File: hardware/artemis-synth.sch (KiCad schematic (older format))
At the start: 41 parts, among them IC1 ATMEGA328P, J1 AVR-ISP-6, J2 CONN JACK STEREO R/A 3PIN 3.5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, SW1 SWITCH_PUSH_CW, SW10 SWITCH_PUSH_CW, SW2 SWITCH_PUSH_CW, SW3 SWITCH_PUSH_CW, SW4 SWITCH_PUSH_CW, SW5 SWITCH_PUSH_CW, SW6 SWITCH_PUSH_CW, SW7 SWITCH_PUSH_CW, SW8 SWITCH_PUSH_CW, SW9 SWITCH_PUSH_CW, U1 MCP4921

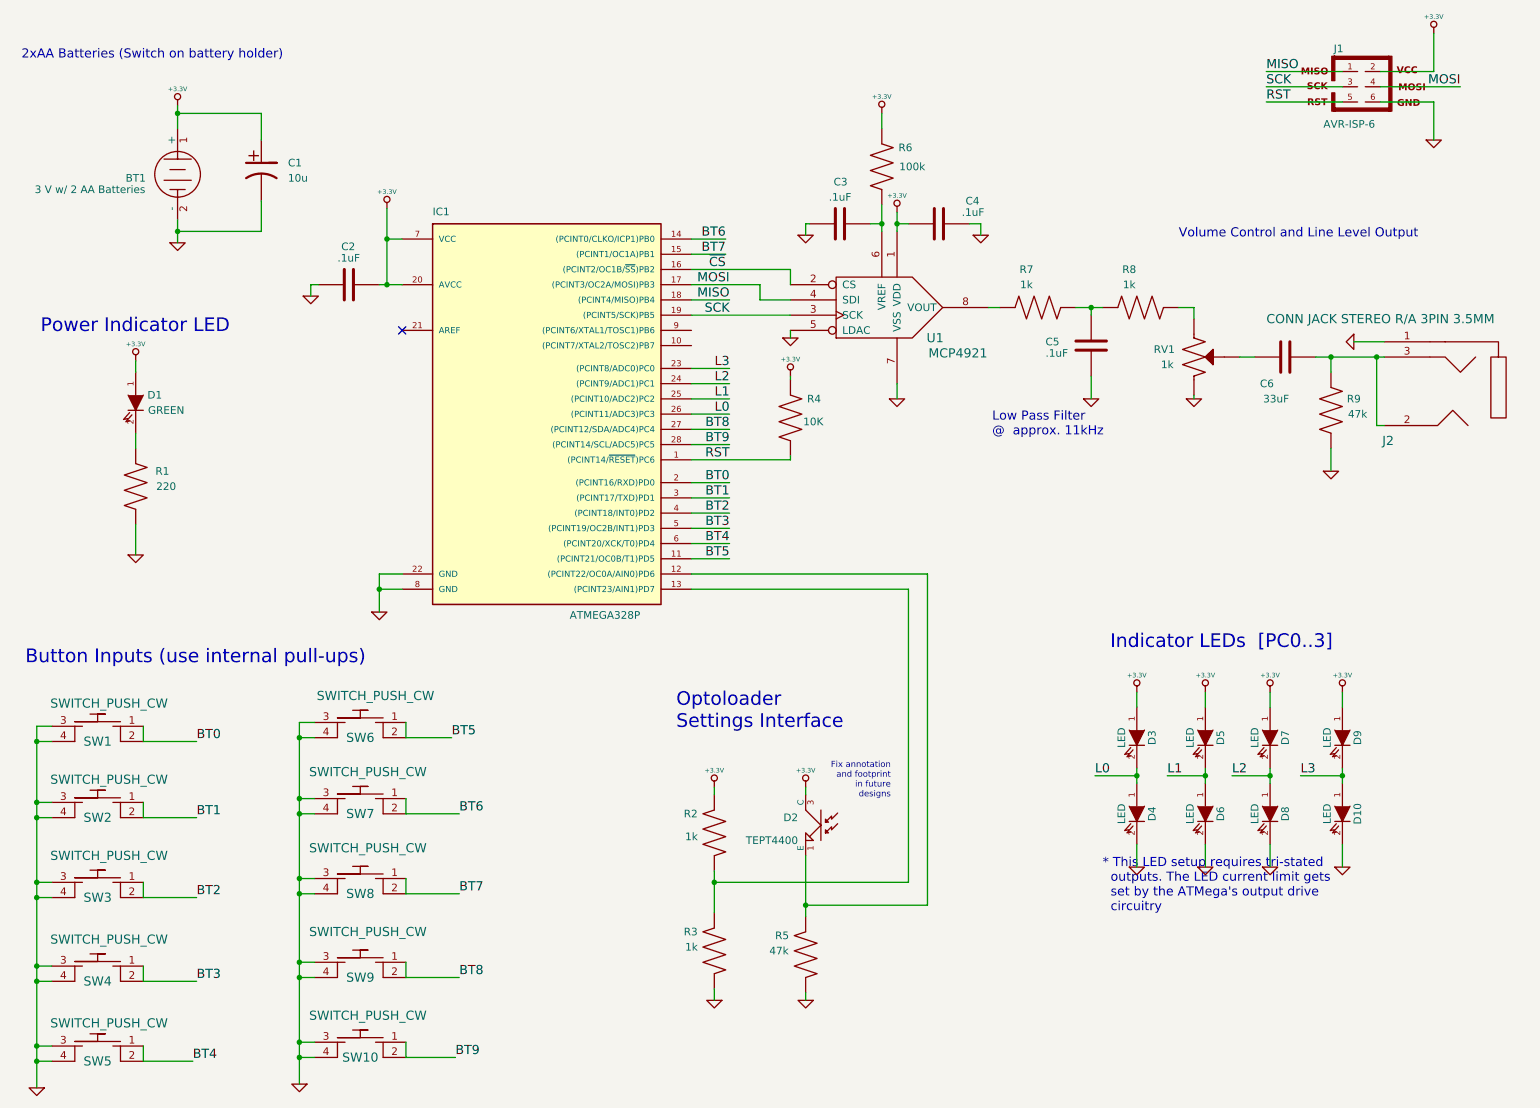
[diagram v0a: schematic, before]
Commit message: Fixed error on D2, in which the collector of the phototransistor was not connected to GND. Also, note that long lead is the Emitter. Fix symbol to make sure it actually represents transistor package correctly...
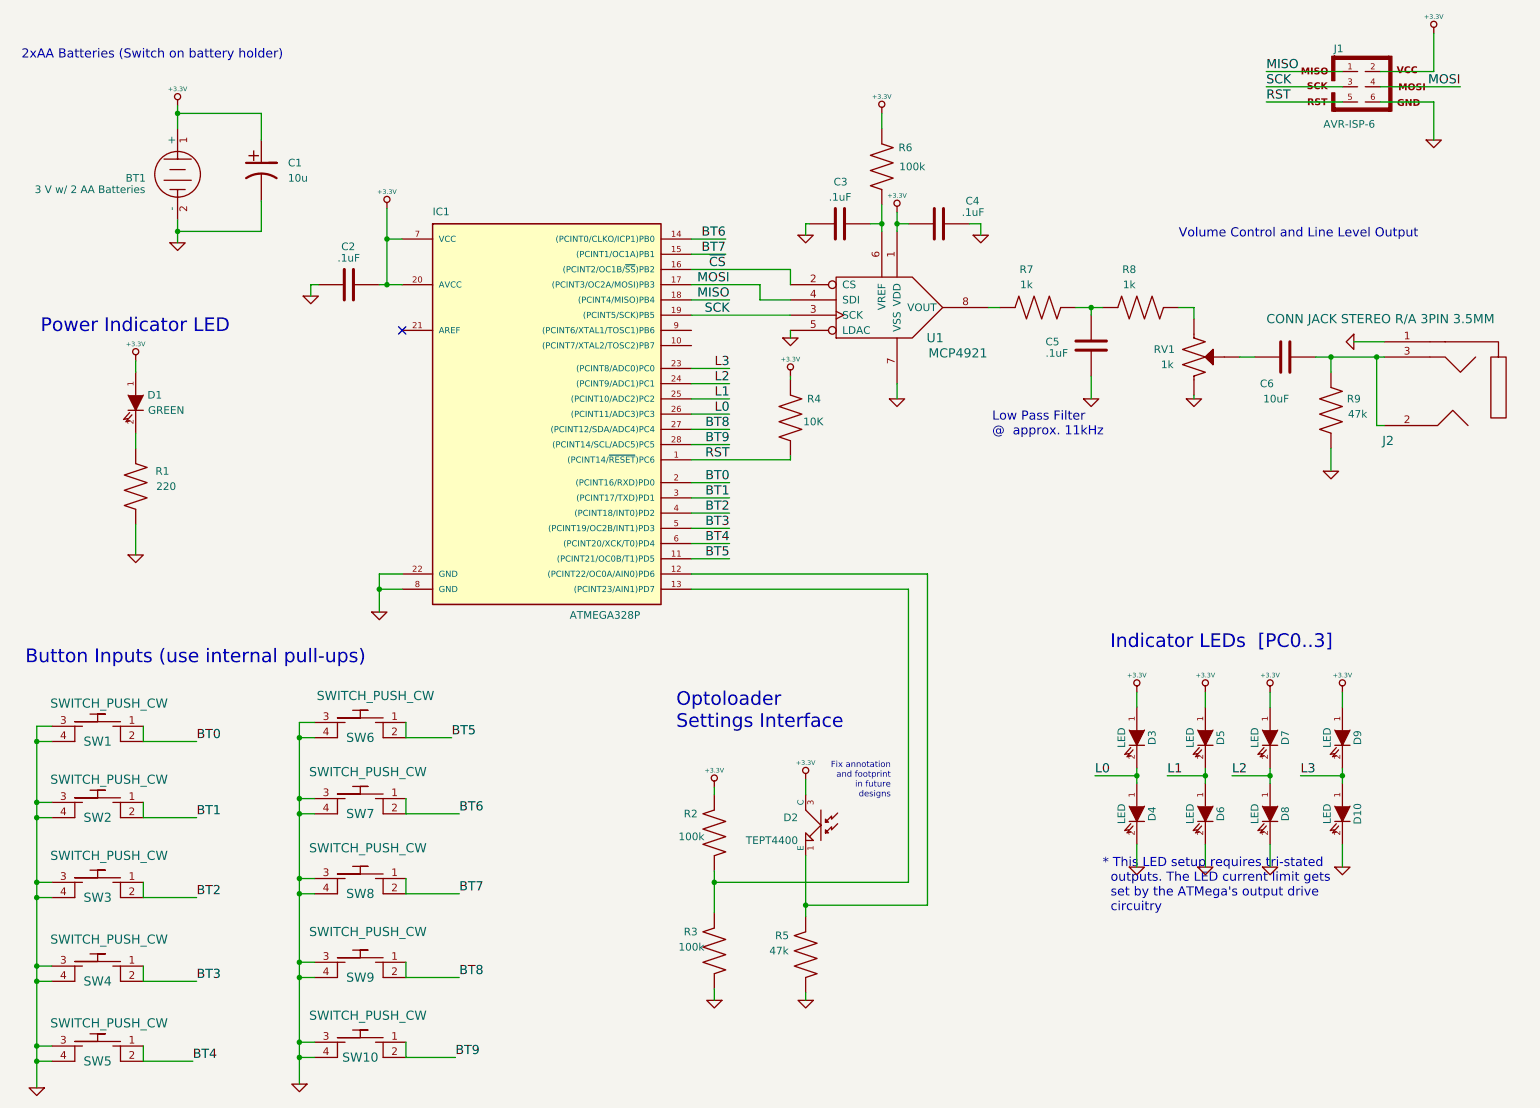
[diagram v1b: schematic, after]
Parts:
- C6: value 33uF -> 10uF
- R2, R3: value 1k -> 100k
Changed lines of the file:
@@
-EESchema Schematic File Version 2  date Fri 05 Jul 2013 12:34:07 PM EDT
+EESchema Schematic File Version 2  date Tue 09 Jul 2013 11:47:29 AM EDT
 LIBS:power
 LIBS:device
@@
 Sheet 1 1
 Title "Artemis Synthesizer"
-Date "5 jul 2013"
+Date "9 jul 2013"
 Rev "B"
 Comp "Christopher Woodall (c) 2012-2013"
@@
 L +3.3V #PWR01
 U 1 1 4FE933FC
-P 5850 5675
-F 0 "#PWR01" H 5850 5635 30  0001 C CNN
-F 1 "+3.3V" H 5850 5785 30  0000 C CNN
-	1    5850 5675
+P 5850 5625
+F 0 "#PWR01" H 5850 5585 30  0001 C CNN
+F 1 "+3.3V" H 5850 5735 30  0000 C CNN
+	1    5850 5625
 	-1   0    0    -1
 $EndComp
@@
 P 5250 5975
 F 0 "R2" H 5405 6100 50  0000 C CNN
-F 1 "1k" H 5400 5950 50  0000 C CNN
+F 1 "100k" H 5400 5950 50  0000 C CNN
 F 2 "R4" H 5400 6050 50  0001 C CNN
 	1    5250 5975
@@
 P 5250 6750
 F 0 "R3" H 5405 6875 50  0000 C CNN
-F 1 "1k" H 5400 6775 50  0000 C CNN
+F 1 "100k" H 5400 6775 50  0000 C CNN
 F 2 "R4" H 5400 6875 50  0001 C CNN
 	1    5250 6750
@@
 P 9000 2850
 F 0 "C6" V 8825 2925 50  0000 L CNN
-F 1 "33uF" V 8725 2825 50  0000 L CNN
+F 1 "10uF" V 8725 2825 50  0000 L CNN
 F 2 "C1V8" H 8825 2850 50  0001 C CNN
 	1    9000 2850
@@
 	800  7475 900  7475
 Wire Wire Line
-	800  5275 800  5375
-Wire Wire Line
-	800  5375 800  5775
-Wire Wire Line
-	800  5775 800  5875
-Wire Wire Line
-	800  5875 800  6300
-Wire Wire Line
-	800  6300 800  6400
-Wire Wire Line
-	800  6400 800  6850
-Wire Wire Line
-	800  6850 800  6950
-Wire Wire Line
-	800  6950 800  7375
-Wire Wire Line
-	800  7375 800  7475
-Wire Wire Line
-	800  7475 800  7650
+	800  5275 800  7650
 Wire Wire Line
 	800  5275 900  5275
@@
 	2525 7350 2625 7350
 Wire Wire Line
-	1725 1950 1725 2025
-Wire Wire Line
-	1725 2025 1725 2100
+	1725 1950 1725 2100
 Wire Wire Line
 	5100 4075 5350 4075
@@
 	5850 1975 5850 2050
 Wire Wire Line
-	6350 1850 6350 1975
-Wire Wire Line
-	6350 1975 6350 2025
+	6350 1850 6350 2025
 Connection ~ 3100 2375
 Wire Wire Line
-	3050 2375 3100 2375
-Wire Wire Line
-	3100 2375 3200 2375
+	3050 2375 3200 2375
 Wire Wire Line
 	6350 1350 6350 1350
@@
 	3200 4275 3050 4275
 Wire Wire Line
-	3050 4275 3050 4375
-Wire Wire Line
-	3050 4375 3050 4525
+	3050 4275 3050 4525
 Wire Wire Line
 	9625 1075 10150 1075
@@
 Connection ~ 3050 4375
 Wire Wire Line
-	3100 1875 3100 2075
-Wire Wire Line
-	3100 2075 3100 2375
+	3100 1875 3100 2375
 Connection ~ 3100 2075
 Wire Wire Line
@@
 	7000 1975 7000 2050
 Wire Wire Line
-	6450 1900 6450 1975
-Wire Wire Line
-	6450 1975 6450 2025
+	6450 1900 6450 2025
 Connection ~ 6450 1975
 Wire Wire Line
 	5350 3875 5100 3875
 Wire Wire Line
-	1725 1200 1725 1250
-Wire Wire Line
-	1725 1250 1725 1350
+	1725 1200 1725 1350
 Wire Wire Line
 	2625 5250 2525 5250
 Wire Wire Line
-	2525 5250 2525 5350
-Wire Wire Line
-	2525 5350 2525 5750
-Wire Wire Line
-	2525 5750 2525 5850
-Wire Wire Line
-	2525 5850 2525 6275
-Wire Wire Line
-	2525 6275 2525 6375
-Wire Wire Line
-	2525 6375 2525 6825
-Wire Wire Line
-	2525 6825 2525 6925
-Wire Wire Line
-	2525 6925 2525 7350
-Wire Wire Line
-	2525 7350 2525 7450
-Wire Wire Line
-	2525 7450 2525 7625
+	2525 5250 2525 7625
 Wire Wire Line
 	2525 7450 2625 7450
@@
 	8900 6050 8900 6200
 Wire Wire Line
-	8025 5550 8025 5600
-Wire Wire Line
-	8025 5600 8025 5650
-Wire Wire Line
-	8475 5550 8475 5600
-Wire Wire Line
-	8475 5600 8475 5650
-Wire Wire Line
-	8900 5550 8900 5600
-Wire Wire Line
-	8900 5600 8900 5650
-Wire Wire Line
-	9375 5550 9375 5600
-Wire Wire Line
-	9375 5600 9375 5650
+	8025 5550 8025 5650
+Wire Wire Line
+	8475 5550 8475 5650
+Wire Wire Line
+	8900 5550 8900 5650
+Wire Wire Line
+	9375 5550 9375 5650
 Wire Wire Line
 	9100 5600 9375 5600
@@
 	5750 2375 5750 2375
 Wire Wire Line
-	5850 5675 5850 5725
-Wire Wire Line
-	5850 6125 5850 6450
-Wire Wire Line
-	5850 6450 5850 6525
+	5850 6125 5850 6525
 Wire Wire Line
 	6350 1350 6350 1250
@@
 	5750 2275 5750 2375
 Wire Wire Line
-	9200 2850 9300 2850
-Wire Wire Line
-	9300 2850 9600 2850
-Wire Wire Line
-	9600 2850 9650 2850
+	9200 2850 9650 2850
 Wire Wire Line
 	9450 2750 9650 2750
@@
 	8400 2525 8300 2525
 Wire Wire Line
-	7625 2525 7725 2525
-Wire Wire Line
-	7725 2525 7800 2525
+	7625 2525 7800 2525
 Wire Wire Line
 	7725 2575 7725 2525
@@
 Connection ~ 9600 2850
 Wire Wire Line
-	5250 6225 5250 6300
-Wire Wire Line
-	5250 6300 5250 6500
+	5250 6225 5250 6500
+Wire Wire Line
+	5850 5625 5850 5725
 $EndSCHEMATC

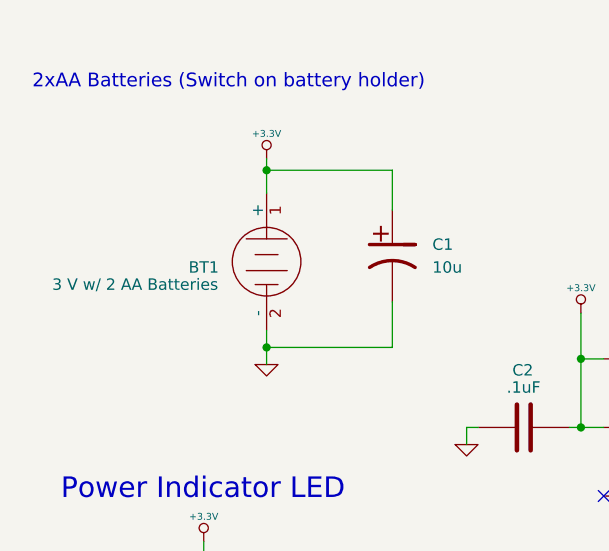
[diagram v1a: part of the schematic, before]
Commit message: Changed D1 Silkscreen. Changed BT1 to BAT1 (battery reference). Changed plane clearance to .02"
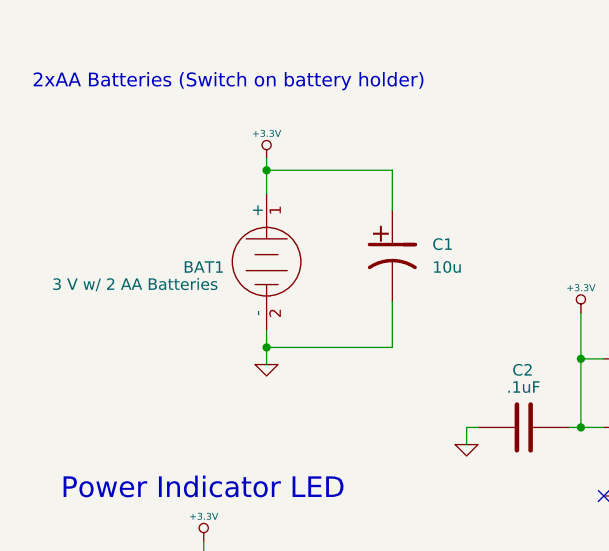
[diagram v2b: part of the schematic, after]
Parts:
- renumbered BT1 to BAT1
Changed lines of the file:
@@
-EESchema Schematic File Version 2  date Tue 09 Jul 2013 11:47:29 AM EDT
+EESchema Schematic File Version 2  date Tue 09 Jul 2013 12:44:30 PM EDT
 LIBS:power
 LIBS:device
@@
 $EndComp
 $Comp
-L BATTERY BT1
+L BATTERY BAT1
 U 1 1 4FE8EE52
 P 1725 1650
-F 0 "BT1" V 1750 1375 50  0000 C CNN
+F 0 "BAT1" V 1750 1375 50  0000 C CNN
 F 1 "3 V w/ 2 AA Batteries" V 1825 1075 50  0000 C CNN
 F 2 "2PIN" H 1725 1560 50  0001 C CNN
